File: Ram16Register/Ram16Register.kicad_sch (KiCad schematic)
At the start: 21 parts, among them J1 Conn_01x16, J10 Conn_01x02, J2 Conn_01x16, J3 Conn_01x08, J4 Conn_01x08, J5 Conn_01x08, J6 Conn_01x08, J7 Conn_01x03, J8 Conn_01x03, J9 Conn_01x02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

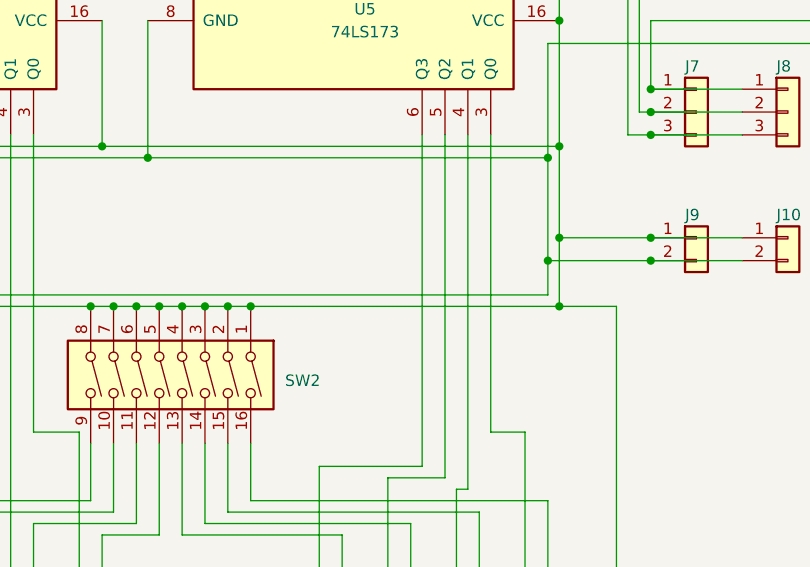
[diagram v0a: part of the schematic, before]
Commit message: Added cappacitor to all Schematic
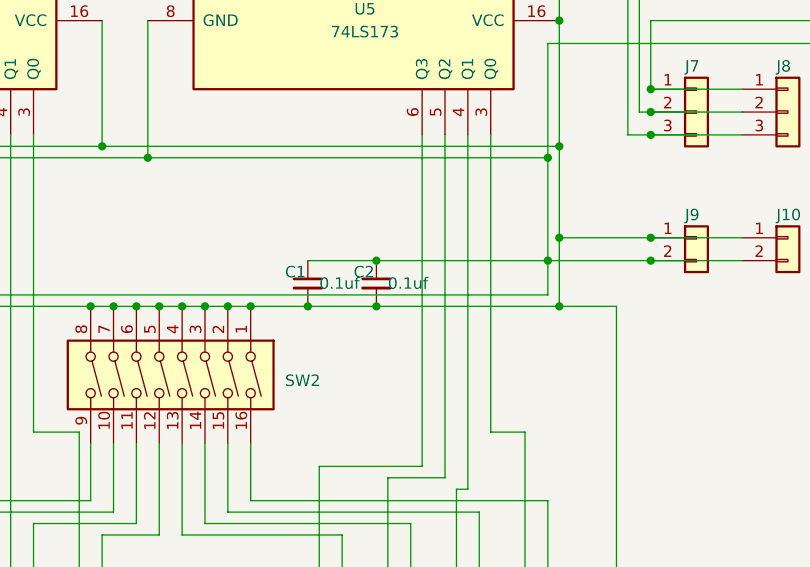
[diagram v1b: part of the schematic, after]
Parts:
- added C1, C2: 0.1uf, symbol Device:C_Small
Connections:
- net at J10.1 (Pin_1), J9.1 (Pin_1), SW1.1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: now also C1.2, C2.2
- net at J10.2 (Pin_2), J9.2 (Pin_2), U1.8 (GND)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: now also C1.1, C2.1
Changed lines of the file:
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@@
   (junction (at 220.98 67.31) (diameter 0) (color 0 0 0 0)
   )
+  (junction (at 201.93 67.31) (diameter 0) (color 0 0 0 0)
+  )
   (junction (at 170.18 72.39) (diameter 0) (color 0 0 0 0)
   )
@@
   (junction (at 123.19 162.56) (diameter 0) (color 0 0 0 0)
   )
+  (junction (at 194.31 72.39) (diameter 0) (color 0 0 0 0)
+  )
   (junction (at 80.01 72.39) (diameter 0) (color 0 0 0 0)
   )
@@
   )
   (junction (at 189.23 17.78) (diameter 0) (color 0 0 0 0)
+  )
+  (junction (at 201.93 72.39) (diameter 0) (color 0 0 0 0)
   )
   (junction (at 220.98 55.88) (diameter 0) (color 0 0 0 0)
@@
     (stroke (width 0) (type default))
   )
+  (wire (pts (xy 194.31 72.39) (xy 201.93 72.39))
+    (stroke (width 0) (type default))
+  )
   (wire (pts (xy 114.3 146.05) (xy 114.3 143.51))
     (stroke (width 0) (type default))
@@
     (stroke (width 0) (type default))
   )
+  (wire (pts (xy 201.93 72.39) (xy 222.25 72.39))
+    (stroke (width 0) (type default))
+  )
   (wire (pts (xy 120.65 153.67) (xy 120.65 162.56))
     (stroke (width 0) (type default))
@@
     (stroke (width 0) (type default))
   )
-  (wire (pts (xy 187.96 72.39) (xy 222.25 72.39))
-    (stroke (width 0) (type default))
-  )
   (wire (pts (xy 74.93 40.64) (xy 74.93 55.88))
     (stroke (width 0) (type default))
@@
     (stroke (width 0) (type default))
   )
+  (wire (pts (xy 187.96 72.39) (xy 194.31 72.39))
+    (stroke (width 0) (type default))
+  )
   (wire (pts (xy 262.89 24.13) (xy 262.89 40.64))
     (stroke (width 0) (type default))
@@
   )
   (wire (pts (xy 163.83 143.51) (xy 163.83 151.13))
+    (stroke (width 0) (type default))
+  )
+  (wire (pts (xy 201.93 67.31) (xy 220.98 67.31))
+    (stroke (width 0) (type default))
+  )
+  (wire (pts (xy 194.31 67.31) (xy 201.93 67.31))
     (stroke (width 0) (type default))
   )
@@
     )
   )
+  (symbol (lib_id "Device:C_Small") (at 194.31 69.85 0) (unit 1)
+    (in_bom yes) (on_board yes) (dnp no)
+    (property "Reference" "C1" (at 191.77 68.58 0)
+      (effects (font (size 1.27 1.27)) (justify left))
+    )
+    (property "Value" "0.1uf" (at 195.58 69.85 0)
+      (effects (font (size 1.27 1.27)) (justify left))
+    )
+    (property "Footprint" "" (at 194.31 69.85 0)
+      (effects (font (size 1.27 1.27)) hide)
+    )
+    (property "Datasheet" "~" (at 194.31 69.85 0)
+      (effects (font (size 1.27 1.27)) hide)
+    )
+    (pin "1")
+    (pin "2")
+    (instances
+      (project "Ram16Register"
+        (path "/5fe22f3b-b680-4748-8026-329c7dedf25b"
+          (reference "C1") (unit 1)
+        )
+      )
+    )
+  )
   (symbol (lib_id "Connector_Generic:Conn_01x08") (at 273.05 73.66 0) (unit 1)
     (in_bom yes) (on_board yes) (dnp no) (fields_autoplaced)
@@
         )
       )
+    )
+  )
+  (symbol (lib_id "Device:C_Small") (at 201.93 69.85 0) (unit 1)
+    (in_bom yes) (on_board yes) (dnp no)
+    (property "Reference" "C2" (at 199.39 68.58 0)
+      (effects (font (size 1.27 1.27)) (justify left))
+    )
+    (property "Value" "0.1uf" (at 203.2 69.85 0)
+      (effects (font (size 1.27 1.27)) (justify left))
+    )
+    (property "Footprint" "" (at 201.93 69.85 0)
+      (effects (font (size 1.27 1.27)) hide)
+    )
+    (property "Datasheet" "~" (at 201.93 69.85 0)
+      (effects (font (size 1.27 1.27)) hide)
+    )
+    (pin "1")
+    (pin "2")
+    (instances
+      (project "Ram16Register"
+        (path "/5fe22f3b-b680-4748-8026-329c7dedf25b"
+          (reference "C2") (unit 1)
+        )
+      )

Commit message: Started assigning footprint
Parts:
- added J11: Connect 3, Connector_PinHeader_2.54mm:PinHeader_1x03_P2.54mm_Vertical, symbol Connector_Generic:Conn_01x03
- C1, C2: footprint (none) -> Capacitor_SMD:C_0603_1608Metric_Pad1.08x0.95mm_HandSolder
- J1, J2: footprint (none) -> Connector_PinHeader_2.54mm:PinHeader_1x16_P2.54mm_Vertical
- J10, J9: footprint (none) -> Connector_PinHeader_2.54mm:PinHeader_1x02_P2.54mm_Vertical
- J3, J4, J5, J6: footprint (none) -> Connector_PinHeader_2.54mm:PinHeader_1x08_P2.54mm_Vertical
- J7, J8: footprint (none) -> Connector_PinHeader_2.54mm:PinHeader_1x03_P2.54mm_Vertical
- SW1, SW2: footprint (none) -> Package_DIP:DIP-8_W7.62mm
- U1, U2, U3, U4: footprint (none) -> Package_SO:TSSOP-16_4.4x5mm_P0.65mm
- U5, U6, U7, U8: footprint (none) -> Package_SO:SOIC-16_3.9x9.9mm_P1.27mm
- U9: footprint (none) -> Package_SO:TSOP-5_1.65x3.05mm_P0.95mm
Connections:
- net at C1.2, C2.2, J10.1 (Pin_1)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: now also J11.1 (Pin_1)
- net at C1.1, C2.1, J10.2 (Pin_2)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: now also U1.15 (E), U2.15 (E), U3.15 (E), U4.15 (E), J11.3 (Pin_3)
- net at U2.1 (S): now also U1.1 (S), U3.1 (S), U4.1 (S), J11.2 (Pin_2)
